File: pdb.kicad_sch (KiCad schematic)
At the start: 9 parts, among them J5 Conn_01x15_Socket, J6 Conn_01x15_Socket, J7 XT-90

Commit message: Finish proof of concept PDB
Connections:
- net SIG1: now also J5.11 (Pin_11); no longer J6.12 (Pin_12)
- net SIG2: now also J5.12 (Pin_12); no longer J6.11 (Pin_11)
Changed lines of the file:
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@@
+	(wire
+		(pts
+			(xy 166.37 100.33) (xy 176.53 100.33)
+		)
+		(stroke
+			(width 0)
+			(type default)
+		)
+	)
 	(wire
 		(pts
@@
 	(wire
 		(pts
-			(xy 220.98 85.09) (xy 210.82 85.09)
+			(xy 176.53 102.87) (xy 166.37 102.87)
 		)
 		(stroke
@@
 	(wire
 		(pts
-			(xy 210.82 82.55) (xy 220.98 82.55)
-		)
-		(stroke
-			(width 0)
-			(type default)
-		)
-	)
-	(wire
-		(pts
 			(xy 132.08 109.22) (xy 128.27 109.22)
 		)
@@
 			(width 0)
 			(type default)
-		)
-	)
-	(label "SIG1"
-		(at 220.98 82.55 180)
-		(effects
-			(font
-				(size 1.27 1.27)
-			)
-			(justify right bottom)
 		)
 	)
@@
 		)
 	)
-	(label "SIG2"
-		(at 220.98 85.09 180)
-		(effects
-			(font
-				(size 1.27 1.27)
-			)
-			(justify right bottom)
-		)
-	)
 	(label "SIG4"
 		(at 95.25 135.89 0)
@@
 	)
 	(label "SIG1"
+		(at 166.37 100.33 0)
+		(effects
+			(font
+				(size 1.27 1.27)
+			)
+			(justify left bottom)
+		)
+	)
+	(label "SIG1"
 		(at 95.25 67.31 0)
 		(effects
@@
 		(effects
 			(font
+				(size 1.27 1.27)
+			)
+			(justify left bottom)
+		)
+	)
+	(label "SIG2"
+		(at 166.37 102.87 0)
+		(effects
+			(font

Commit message: Prepare for PDR
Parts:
- removed J5, J6: Conn_01x15_Socket, Connector_PinHeader_2.54mm:PinHeader_1x15_P2.54mm_Vertical, symbol Connector:Conn_01x15_Socket
- added C27: 0.1u, Capacitor_SMD:C_0805_2012Metric, symbol Device:C_Small
- added C28: 10u, Capacitor_SMD:C_0805_2012Metric, symbol Device:C_Small
- added J20: XT-90, footprints:XT90_V, symbol Connector_Generic:Conn_01x02
- added J30, J31, J32, J33: XT-30, Connector_AMASS:AMASS_XT30UPB-F_1x02_P5.0mm_Vertical, symbol Connector_Generic:Conn_01x02
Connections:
- net GND2: now also C27.2, C28.2, J20.1 (Pin_1), J30.1 (Pin_1), J31.1 (Pin_1), J32.1 (Pin_1), J33.1 (Pin_1)
- net +BATT renamed +ACT
- net +ACT: now also J32.2 (Pin_2), J33.2 (Pin_2)
- new net +LOG: C27.1, C28.1, J20.2 (Pin_2), J30.2 (Pin_2), J31.2 (Pin_2)
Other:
- added sheet BDC5 (productionBDC.kicad_sch)
- added sheet BDC6 (productionBDC.kicad_sch)
- sheet BDC1 ports: added none; removed SIG, VOUT
- sheet BDC2 ports: added none; removed SIG, VOUT
- sheet BDC3 ports: added none; removed SIG, VOUT
- sheet BDC4 ports: added none; removed SIG, VOUT
- note added: "Actuator (servos, motors, ect.) power line"
- note added: "Logic (Cube Orange, Jetson, ect.) power line"

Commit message: Add JST B2B-XH connectors
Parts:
- J31, J32: footprint Connector_AMASS:AMASS_XT30UPB-F_1x02_P5.0mm_Vertical -> footprints:CONN_B2B-XH-ALFSN_JST
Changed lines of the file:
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@@
 			)
 		)
-		(property "Footprint" "Connector_AMASS:AMASS_XT30UPB-F_1x02_P5.0mm_Vertical"
+		(property "Footprint" "footprints:CONN_B2B-XH-ALFSN_JST"
 			(at 227.33 64.77 0)
 			(effects
@@
 			)
 		)
-		(property "Footprint" "Connector_AMASS:AMASS_XT30UPB-F_1x02_P5.0mm_Vertical"
+		(property "Footprint" "footprints:CONN_B2B-XH-ALFSN_JST"
 			(at 207.01 82.55 0)
 			(effects

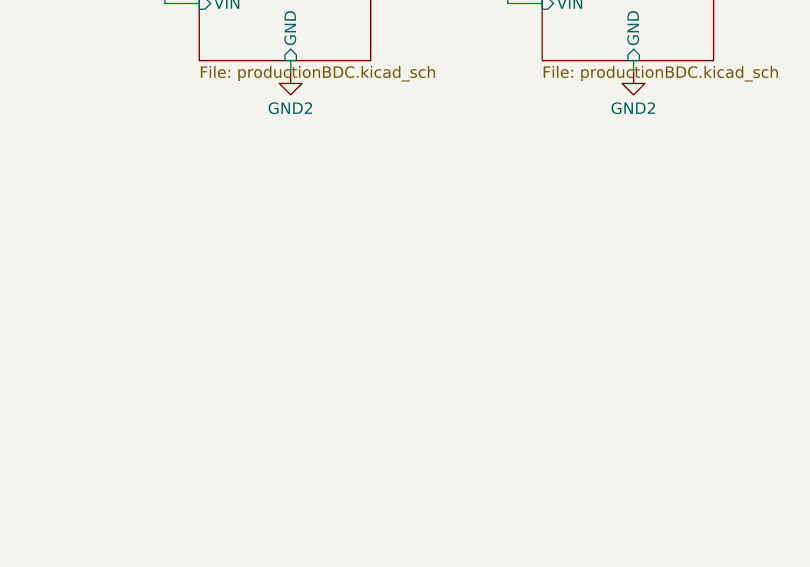
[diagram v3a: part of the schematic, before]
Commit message: Update to KiCad 10
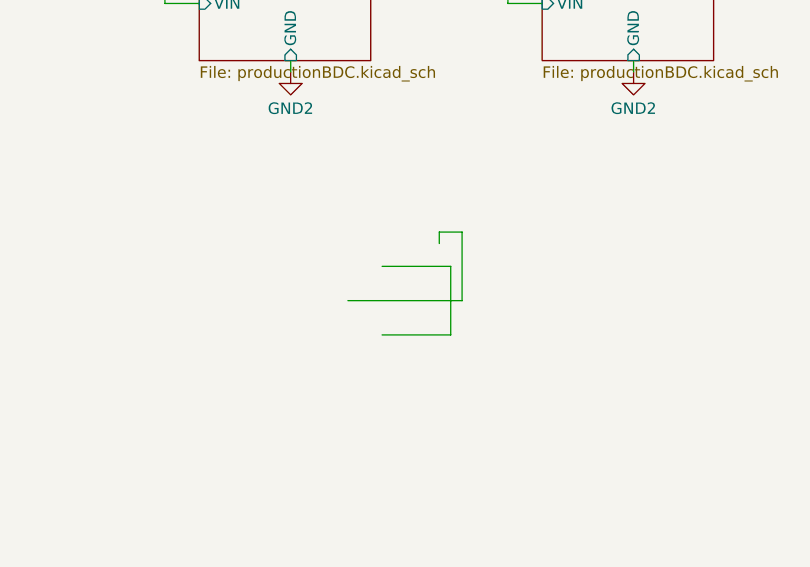
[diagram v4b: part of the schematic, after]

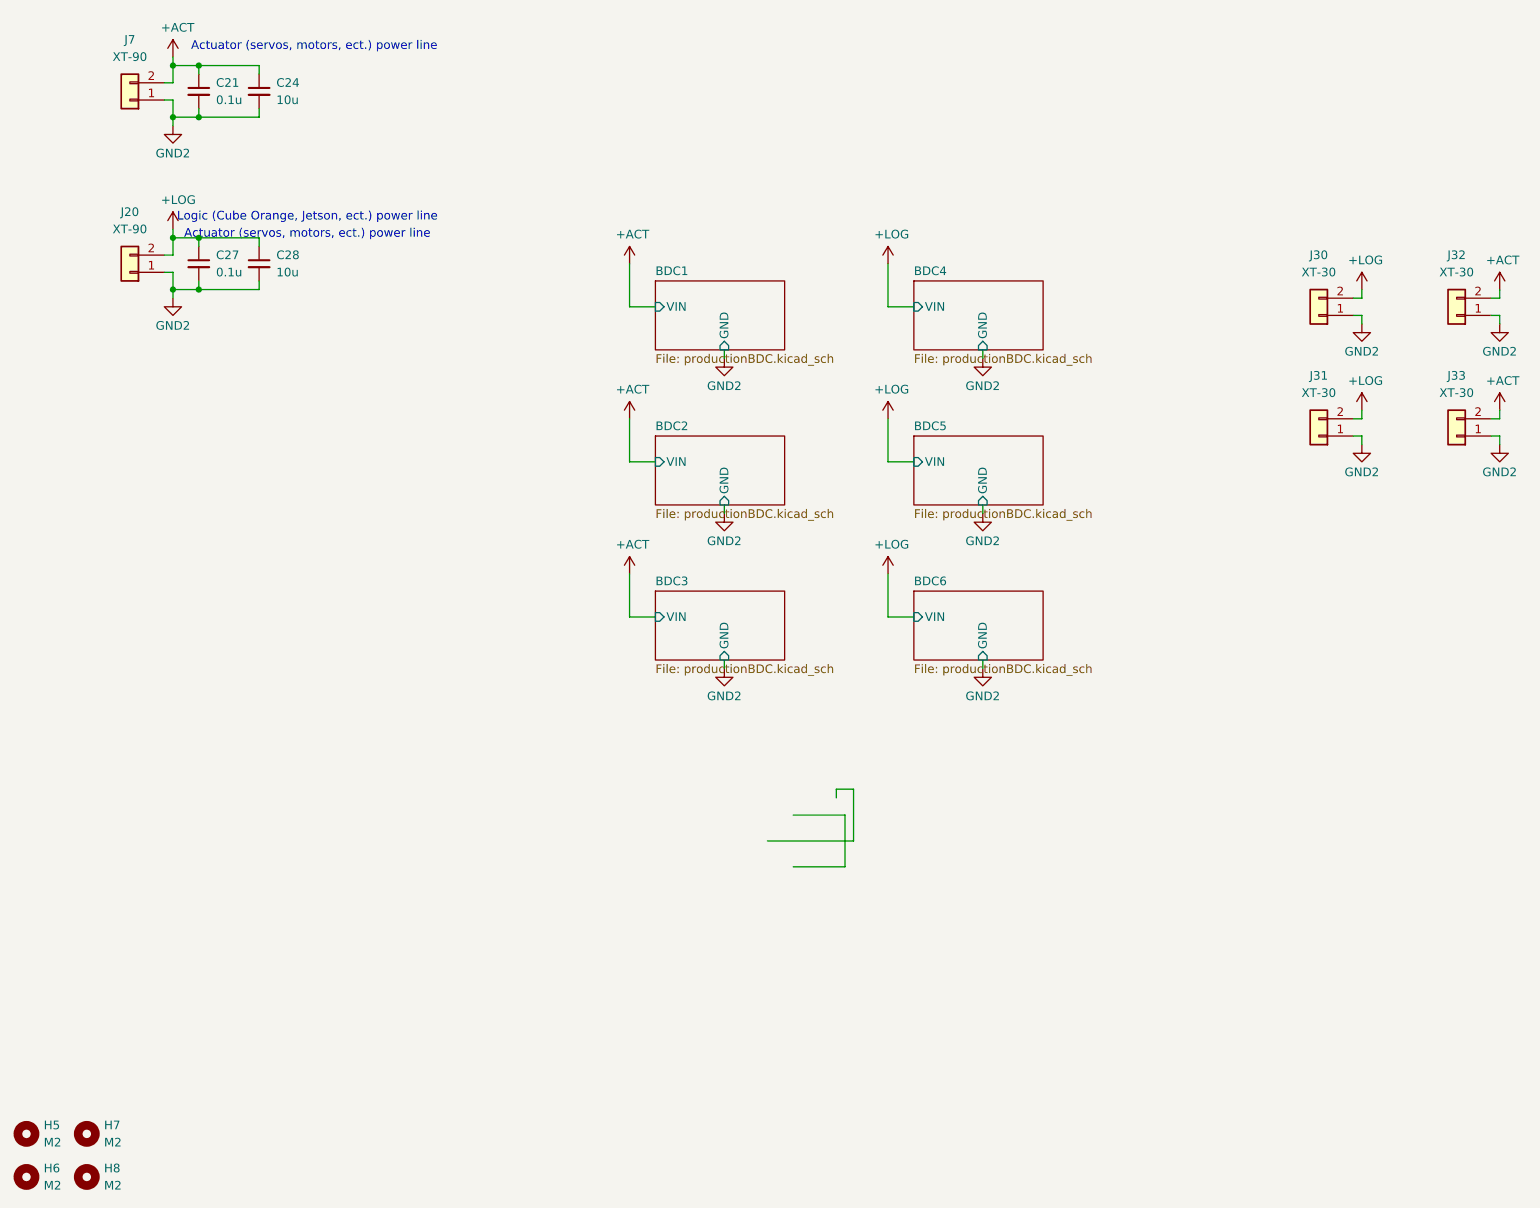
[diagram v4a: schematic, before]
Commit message: Add motor connectors
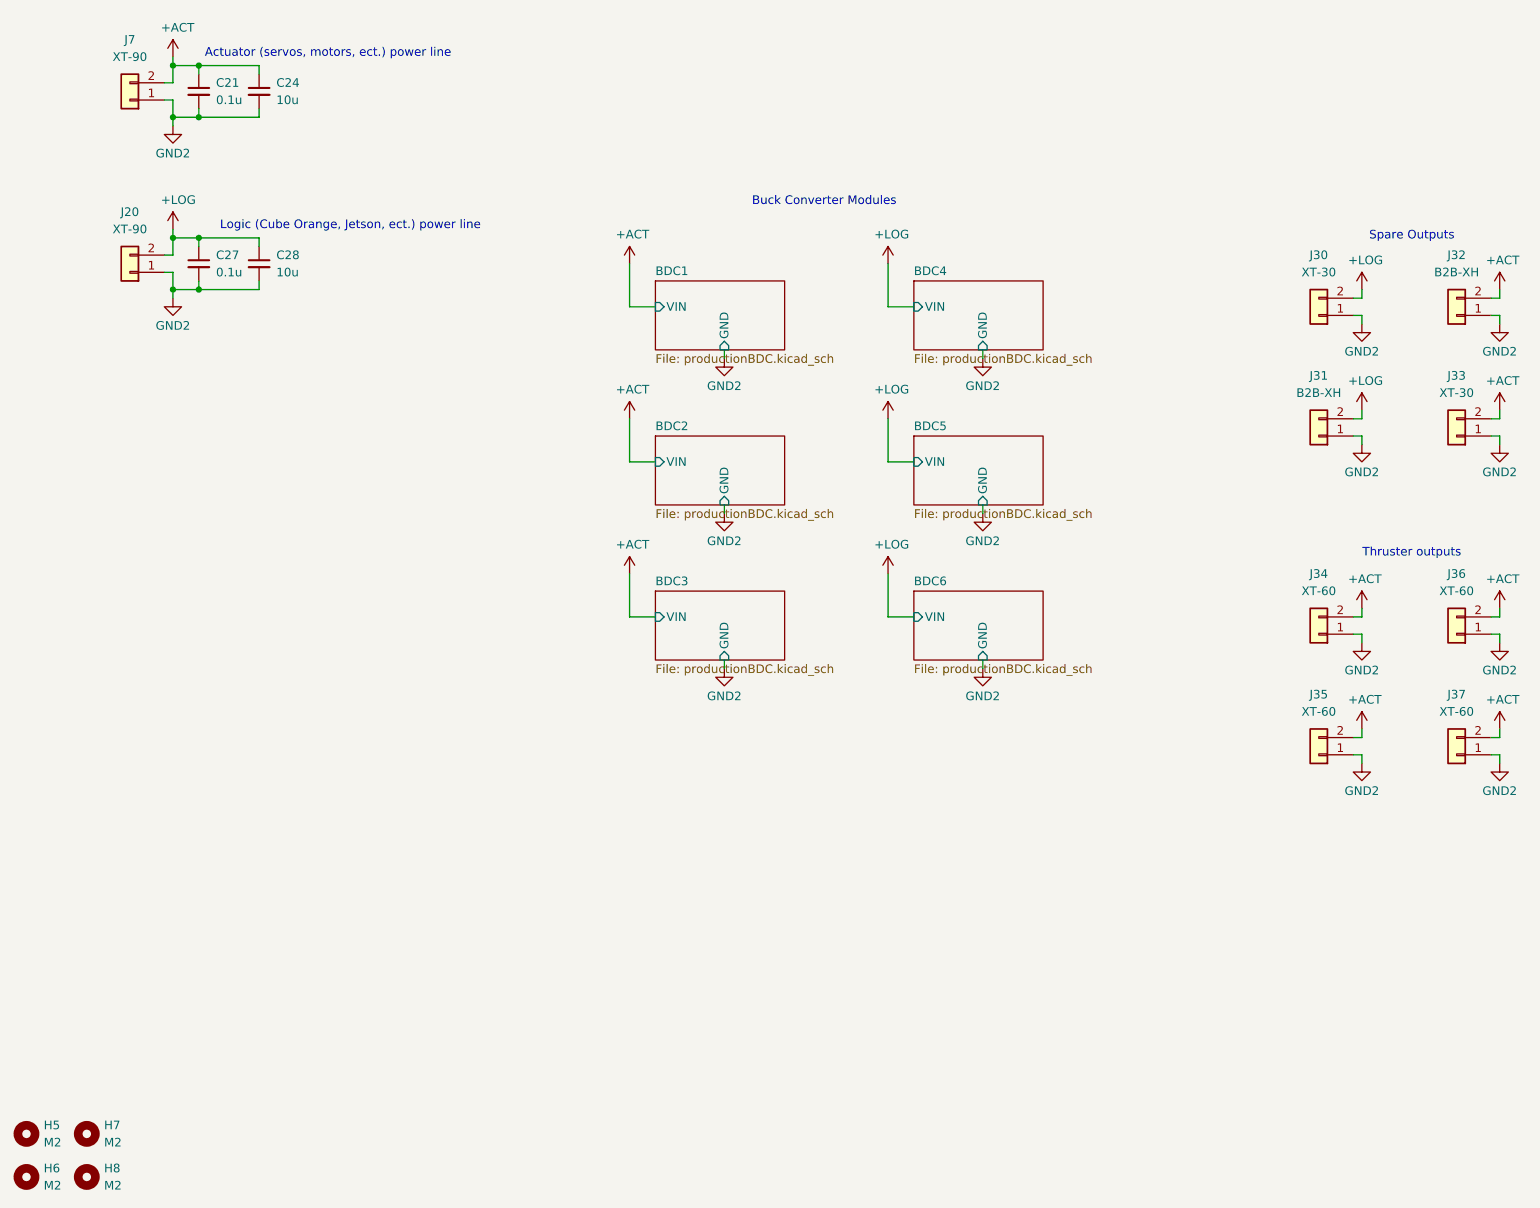
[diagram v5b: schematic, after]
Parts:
- added J34, J35, J36, J37: XT-60, footprints:AMASS_XT60-F_1x02_P7.20mm_Vertical, symbol Connector_Generic:Conn_01x02
- J31, J32: value XT-30 -> B2B-XH
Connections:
- net +ACT: now also J34.2 (Pin_2), J35.2 (Pin_2), J36.2 (Pin_2), J37.2 (Pin_2)
- net GND2: now also J34.1 (Pin_1), J35.1 (Pin_1), J36.1 (Pin_1), J37.1 (Pin_1)
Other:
- note added: "Buck Converter Modules"
- note added: "Spare Outputs"
- note added: "Thruster outputs"

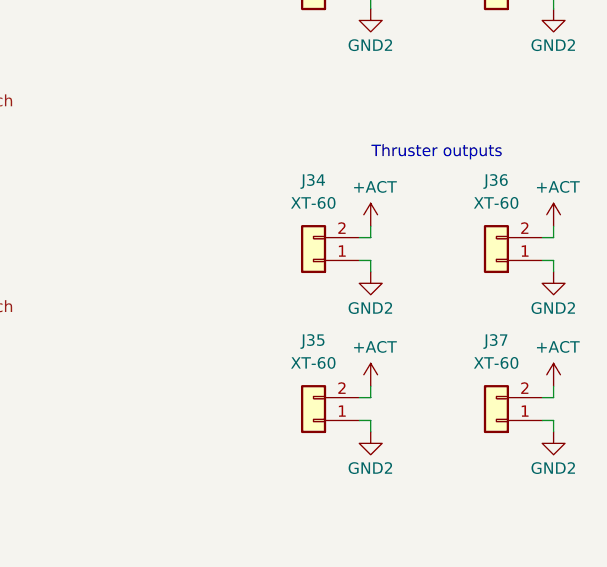
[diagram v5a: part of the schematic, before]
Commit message: Switch ESC connectors to XT-30
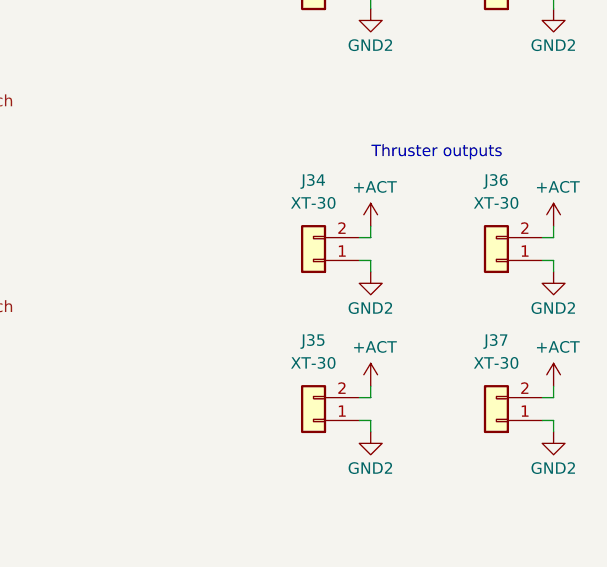
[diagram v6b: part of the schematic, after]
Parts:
- J34, J35, J36, J37: value XT-60 -> XT-30; footprint footprints:AMASS_XT60-F_1x02_P7.20mm_Vertical -> Connector_AMASS:AMASS_XT30UPB-F_1x02_P5.0mm_Vertical
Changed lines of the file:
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@@
 			)
 		)
-		(property "Value" "XT-60"
+		(property "Value" "XT-30"
 			(at 227.33 123.19 0)
 			(show_name no)
@@
 			)
 		)
-		(property "Footprint" "footprints:AMASS_XT60-F_1x02_P7.20mm_Vertical"
+		(property "Footprint" "Connector_AMASS:AMASS_XT30UPB-F_1x02_P5.0mm_Vertical"
 			(at 227.33 129.54 0)
 			(hide yes)
@@
 			)
 		)
-		(property "Value" "XT-60"
+		(property "Value" "XT-30"
 			(at 227.33 105.41 0)
 			(show_name no)
@@
 			)
 		)
-		(property "Footprint" "footprints:AMASS_XT60-F_1x02_P7.20mm_Vertical"
+		(property "Footprint" "Connector_AMASS:AMASS_XT30UPB-F_1x02_P5.0mm_Vertical"
 			(at 227.33 111.76 0)
 			(hide yes)
@@
 			)
 		)
-		(property "Value" "XT-60"
+		(property "Value" "XT-30"
 			(at 207.01 105.41 0)
 			(show_name no)
@@
 			)
 		)
-		(property "Footprint" "footprints:AMASS_XT60-F_1x02_P7.20mm_Vertical"
+		(property "Footprint" "Connector_AMASS:AMASS_XT30UPB-F_1x02_P5.0mm_Vertical"
 			(at 207.01 111.76 0)
 			(hide yes)
@@
 			)
 		)
-		(property "Value" "XT-60"
+		(property "Value" "XT-30"
 			(at 207.01 123.19 0)
 			(show_name no)
@@
 			)
 		)
-		(property "Footprint" "footprints:AMASS_XT60-F_1x02_P7.20mm_Vertical"
+		(property "Footprint" "Connector_AMASS:AMASS_XT30UPB-F_1x02_P5.0mm_Vertical"
 			(at 207.01 129.54 0)
 			(hide yes)
